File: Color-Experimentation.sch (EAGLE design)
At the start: 26 parts, among them J1 10118193-0001LF, U2 ATTINY85-20MUR

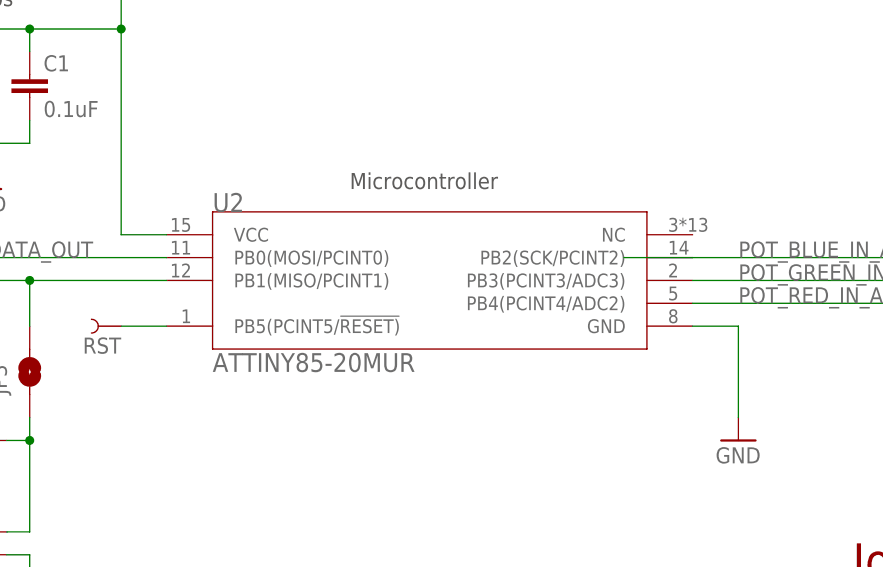
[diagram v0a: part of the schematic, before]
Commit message: Switch microcontroller for availability: v1.1
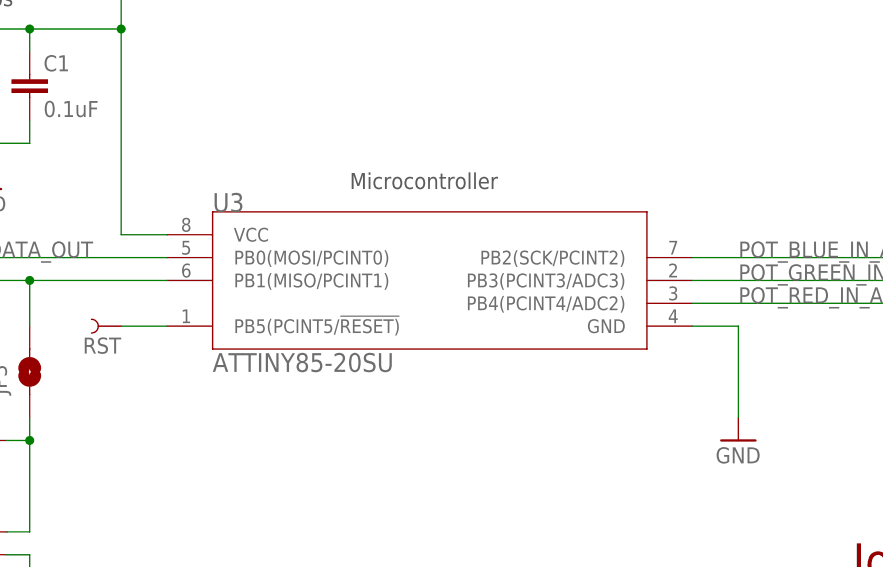
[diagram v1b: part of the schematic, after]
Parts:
- removed U2: ATTINY85-20MUR, Color-Experimentation:ATTINY85-20MUR
- added U3: ATTINY85-20SU, Color-Experimentation:ATTINY85-20SU
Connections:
- net GND: now also U3.GND; no longer U2.GND
- net LED_DATA_OUT: now also U3.PB0(MOSI/PCINT0); no longer U2.PB0(MOSI/PCINT0)
- net N$4: now also U3.PB5(PCINT5/!RESET); no longer U2.PB5(PCINT5/!RESET)
- net N$6: now also U3.PB1(MISO/PCINT1); no longer U2.PB1(MISO/PCINT1)
- net POT_BLUE_IN_A: now also U3.PB2(SCK/PCINT2); no longer U2.PB2(SCK/PCINT2)
- net POT_GREEN_IN_A: now also U3.PB3(PCINT3/ADC3); no longer U2.PB3(PCINT3/ADC3)
- net POT_RED_IN_A: now also U3.PB4(PCINT4/ADC2); no longer U2.PB4(PCINT4/ADC2)
- net V_USB: now also U3.VCC; no longer U2.VCC
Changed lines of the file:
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@@
 </classes>
 <parts>
-<part name="U2" library="Color-Experimentation" library_urn="urn:adsk.eagle:library:32037284" deviceset="ATTINY85-20MUR" device="" package3d_urn="urn:adsk.eagle:package:32037311/2"/>
 <part name="GND14" library="Color-Experimentation" library_urn="urn:adsk.eagle:library:32037284" deviceset="GND" device=""/>
 <part name="SUPPLY1" library="Color-Experimentation" library_urn="urn:adsk.eagle:library:32037284" deviceset="V_USB" device=""/>
@@
 <part name="SUPPLY6" library="Color-Experimentation" library_urn="urn:adsk.eagle:library:32037284" deviceset="V_USB" device=""/>
 <part name="JP3" library="Color-Experimentation" library_urn="urn:adsk.eagle:library:32037284" deviceset="JUMPER-SMT_2_NO" device="_SILK" package3d_urn="urn:adsk.eagle:package:32037310/2"/>
+<part name="U3" library="Color-Experimentation" library_urn="urn:adsk.eagle:library:32037284" deviceset="ATTINY85-20SU" device=""/>
 </parts>
 <sheets>
@@
 </plain>
 <instances>
-<instance part="U2" gate="A" x="386.08" y="111.76" smashed="yes">
-<attribute name="NAME" x="360.68" y="119.38" size="2.0828" layer="95" ratio="6" rot="SR0"/>
-<attribute name="VALUE" x="360.68" y="101.6" size="2.0828" layer="96" ratio="6" rot="SR0"/>
-</instance>
 <instance part="GND14" gate="1" x="419.1" y="93.98" smashed="yes">
 <attribute name="VALUE" x="416.56" y="91.44" size="1.778" layer="96"/>
@@
 <attribute name="NAME" x="337.82" y="99.06" size="1.778" layer="95" font="vector" rot="R90"/>
 </instance>
+<instance part="U3" gate="G$1" x="386.08" y="111.76" smashed="yes">
+<attribute name="NAME" x="360.68" y="119.38" size="2.0828" layer="95" ratio="6" rot="SR0"/>
+<attribute name="VALUE" x="360.68" y="101.6" size="2.0828" layer="96" ratio="6" rot="SR0"/>
+</instance>
 </instances>
 <busses>
@@
 <net name="GND" class="1">
 <segment>
-<pinref part="U2" gate="A" pin="GND"/>
 <wire x1="414.02" y1="106.68" x2="419.1" y2="106.68" width="0.1524" layer="91"/>
 <wire x1="419.1" y1="106.68" x2="419.1" y2="96.52" width="0.1524" layer="91"/>
 <pinref part="GND14" gate="1" pin="GND"/>
+<pinref part="U3" gate="G$1" pin="GND"/>
 </segment>
 <segment>
@@
 <net name="V_USB" class="1">
 <segment>
-<pinref part="U2" gate="A" pin="VCC"/>
 <wire x1="355.6" y1="116.84" x2="350.52" y2="116.84" width="0.1524" layer="91"/>
 <pinref part="SUPPLY1" gate="G$1" pin="V_USB"/>
@@
 <wire x1="340.36" y1="137.16" x2="340.36" y2="139.7" width="0.1524" layer="91"/>
 <junction x="340.36" y="139.7"/>
+<pinref part="U3" gate="G$1" pin="VCC"/>
 </segment>
 <segment>
@@
 <net name="LED_DATA_OUT" class="0">
 <segment>
-<pinref part="U2" gate="A" pin="PB0(MOSI/PCINT0)"/>
 <wire x1="355.6" y1="114.3" x2="327.66" y2="114.3" width="0.1524" layer="91"/>
 <label x="330.2" y="114.3" size="1.778" layer="95"/>
 <pinref part="JP2" gate="G$1" pin="2"/>
+<pinref part="U3" gate="G$1" pin="PB0(MOSI/PCINT0)"/>
 </segment>
 <segment>
@@
 </segment>
 <segment>
-<pinref part="U2" gate="A" pin="PB4(PCINT4/ADC2)"/>
 <wire x1="414.02" y1="109.22" x2="436.88" y2="109.22" width="0.1524" layer="91"/>
 <label x="419.1" y="109.22" size="1.778" layer="95"/>
+<pinref part="U3" gate="G$1" pin="PB4(PCINT4/ADC2)"/>
 </segment>
 </net>
 <net name="POT_GREEN_IN_A" class="0">
 <segment>
-<pinref part="U2" gate="A" pin="PB3(PCINT3/ADC3)"/>
 <wire x1="414.02" y1="111.76" x2="436.88" y2="111.76" width="0.1524" layer="91"/>
 <label x="419.1" y="111.76" size="1.778" layer="95"/>
+<pinref part="U3" gate="G$1" pin="PB3(PCINT3/ADC3)"/>
 </segment>
 <segment>
@@
 </segment>
 <segment>
-<pinref part="U2" gate="A" pin="PB2(SCK/PCINT2)"/>
 <wire x1="414.02" y1="114.3" x2="444.5" y2="114.3" width="0.1524" layer="91"/>
 <label x="419.1" y="114.3" size="1.778" layer="95"/>
 <pinref part="JP1" gate="G$1" pin="1"/>
-<wire x1="406.4" y1="114.3" x2="414.02" y2="114.3" width="0.1524" layer="91"/>
+<pinref part="U3" gate="G$1" pin="PB2(SCK/PCINT2)"/>
 </segment>
 </net>
 <net name="N$4" class="0">
 <segment>
-<pinref part="U2" gate="A" pin="PB5(PCINT5/!RESET)"/>
 <pinref part="RST" gate="G$1" pin="1"/>
 <wire x1="355.6" y1="106.68" x2="350.52" y2="106.68" width="0.1524" layer="91"/>
+<pinref part="U3" gate="G$1" pin="PB5(PCINT5/!RESET)"/>
 </segment>
 </net>
@@
 <net name="N$6" class="0">
 <segment>
-<pinref part="U2" gate="A" pin="PB1(MISO/PCINT1)"/>
 <pinref part="MISO" gate="G$1" pin="1"/>
 <wire x1="355.6" y1="111.76" x2="340.36" y2="111.76" width="0.1524" layer="91"/>
@@
 <wire x1="340.36" y1="106.68" x2="340.36" y2="111.76" width="0.1524" layer="91"/>
 <junction x="340.36" y="111.76"/>
+<pinref part="U3" gate="G$1" pin="PB1(MISO/PCINT1)"/>
 </segment>
 </net>
@@
 </sheet>
 </sheets>
+<errors>
+</errors>
 </schematic>
 </drawing>

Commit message: Various improvements to address #2
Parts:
- removed C3, C4, C5, C6: 0.1uF, Color-Experimentation:CAP_0.1UF_25V_X7R-0603
- removed JP2, JP3: JUMPER-SMT_2_NO_SILK, Color-Experimentation:JUMPER-SMT_2_NO_SILK
- removed R1: 10k, Color-Experimentation:RES_10K_1%R0603
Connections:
- removed net MOSI: JP2.1, MOSI.1
- removed net N$3: J2.1, JP3.1, R1.2
- removed net SCK: JP1.2, SCK.1
- new net N$7: JP1.1, SCK.1, U3.PB2(SCK/PCINT2)
- net GND: no longer C3.2, C4.2, C5.2, C6.2
- net LED_DATA_OUT: now also MOSI.1; no longer JP2.2
- net N$6: now also J2.1; no longer JP3.2
- net POT_BLUE_IN_A: now also JP1.2; no longer JP1.1, U3.PB2(SCK/PCINT2)
- net V_USB: no longer C3.1, C4.1, C5.1, C6.1, R1.1
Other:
- note added: "After programming, close JP1"
- note added: "CHANGELOG v1.1 -> v1.2 - Removed unnecessary solder jumpers - Fixed incorrect placement of JP1. Now correctly disconnects slider pot from SCK for programming. - Removed LED decoupling caps (not needed) - Moved USB connector closer to board edge to solve mech interference - Remove R1 (Mixed LED jumper pullup), use internal pullups in firmware - Moved C1, C2 farther apart to ease assembly"
- note added: "TODO: - Fix slider pot mechanical pins (L/R switch) - Can we support either the SU or MU ATTINY variants simultaneously with overlapping footprints? - Consider adding 3x AAA battery holder? Keystone 2479 looks like it could fit."
- note removed: "After programming, close JP1, JP2, JP3"
- note removed: "LED Decoupling Caps"
- moved on the sheet: GND, J1, J2, JP1, MISO, MOSI, SCK, VCC
